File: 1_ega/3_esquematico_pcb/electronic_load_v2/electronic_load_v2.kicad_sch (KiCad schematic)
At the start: 67 parts, among them J1 Encoder, J11 LOAD, J12 Memoria SD, J13 LCD, J15 VCC, J16 RTC, J17 EGB, J3 GND, J6 RPico PWR, J7 GND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

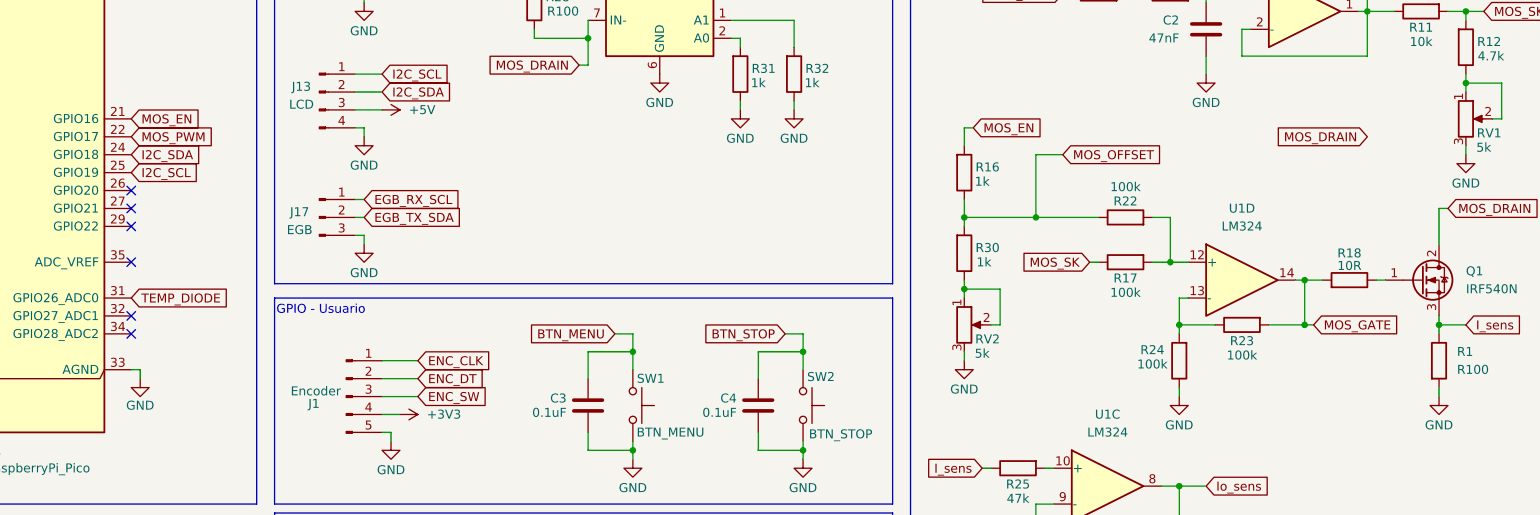
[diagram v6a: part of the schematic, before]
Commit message: add: change Rsense to ina smd size
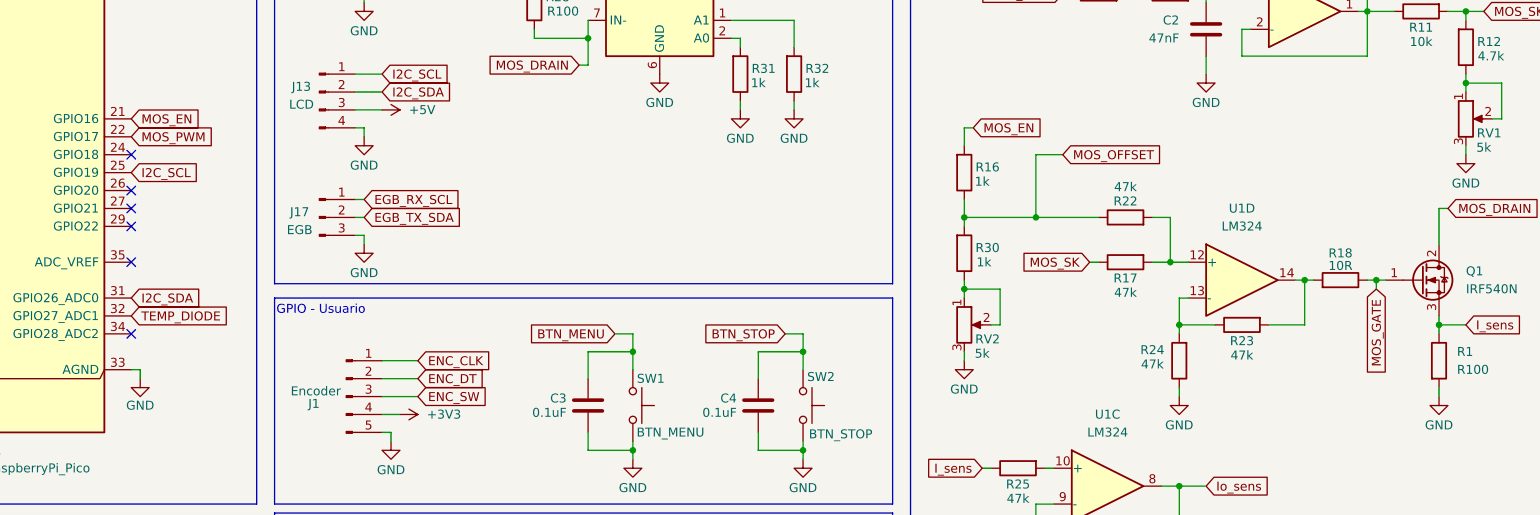
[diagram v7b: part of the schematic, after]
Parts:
- R1: footprint Resistor_THT:R_Axial_DIN0922_L20.0mm_D9.0mm_P25.40mm_Horizontal -> electronic_load:R_shunt_ina219
- R17, R22, R23, R24: value 100k -> 47k
- R20, R21: footprint Resistor_THT:R_Axial_DIN0207_L6.3mm_D2.5mm_P7.62mm_Horizontal -> Resistor_THT:R_Axial_DIN0207_L6.3mm_D2.5mm_P10.16mm_Horizontal
- R31, R32: footprint Resistor_SMD:R_0805_2012Metric_Pad1.20x1.40mm_HandSolder -> Resistor_SMD:R_1206_3216Metric_Pad1.30x1.75mm_HandSolder
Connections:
- net I2C_SDA: now also A1.31 (GPIO26_ADC0); no longer A1.24 (GPIO18)
- net MOS_GATE: now also Q1.1 (G), R18.1; no longer R18.2, R23.2, U1.14
- net TEMP_DIODE: now also A1.32 (GPIO27_ADC1); no longer A1.31 (GPIO26_ADC0)
- new net: R18.2, R23.2, U1.14
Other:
- moved on the sheet: R18
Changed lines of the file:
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@@
 	)
 	(junction
-		(at 67.31 127)
+		(at 254 72.39)
 		(diameter 0)
 		(color 0 0 0 0)
 	)
 	(junction
-		(at 243.84 78.74)
+		(at 67.31 127)
 		(diameter 0)
 		(color 0 0 0 0)
@@
 	)
 	(no_connect
-		(at 77.47 77.47)
-	)
-	(no_connect
 		(at 77.47 80.01)
 	)
@@
 	)
 	(no_connect
+		(at 77.47 54.61)
+	)
+	(no_connect
 		(at 77.47 69.85)
 	)
@@
 	(wire
 		(pts
+			(xy 254 72.39) (xy 255.27 72.39)
+		)
+		(stroke
+			(width 0)
+			(type default)
+		)
+	)
+	(wire
+		(pts
 			(xy 226.06 88.9) (xy 226.06 87.63)
 		)
@@
 	(wire
 		(pts
-			(xy 243.84 72.39) (xy 246.38 72.39)
+			(xy 243.84 72.39) (xy 245.11 72.39)
 		)
 		(stroke
@@
 	(wire
 		(pts
+			(xy 254 72.39) (xy 254 73.66)
+		)
+		(stroke
+			(width 0)
+			(type default)
+		)
+	)
+	(wire
+		(pts
 			(xy 54.61 115.57) (xy 54.61 116.84)
 		)
@@
 	(wire
 		(pts
-			(xy 254 72.39) (xy 255.27 72.39)
+			(xy 252.73 72.39) (xy 254 72.39)
 		)
 		(stroke
@@
 	(wire
 		(pts
-			(xy 243.84 78.74) (xy 245.11 78.74)
-		)
-		(stroke
-			(width 0)
-			(type default)
-		)
-	)
-	(wire
-		(pts
 			(xy 262.89 78.74) (xy 262.89 80.01)
 		)
@@
 	(global_label "I2C_SDA"
 		(shape input)
-		(at 77.47 54.61 0)
+		(at 77.47 74.93 0)
 		(fields_autoplaced yes)
 		(effects
@@
 		)
 		(property "Intersheetrefs" "${INTERSHEET_REFS}"
-			(at 88.0752 54.61 0)
+			(at 88.0752 74.93 0)
 			(effects
 				(font
@@
 		)
 	)
-	(global_label "MOS_DRAIN"
-		(shape input)
-		(at 252.73 52.07 180)
-		(fields_autoplaced yes)
-		(effects
-			(font
-				(size 1.27 1.27)
-			)
-			(justify right)
-		)
-		(property "Intersheetrefs" "${INTERSHEET_REFS}"
-			(at 239.2219 52.07 0)
-			(effects
-				(font
-					(size 1.27 1.27)
-				)
-				(justify right)
-				(hide yes)
-			)
-		)
-	)
 	(global_label "I_sens"
 		(shape input)
@@
 	(global_label "MOS_GATE"
 		(shape input)
-		(at 245.11 78.74 0)
+		(at 254 73.66 270)
 		(fields_autoplaced yes)
 		(effects
@@
 				(size 1.27 1.27)
 			)
-			(justify left)
+			(justify right)
 		)
 		(property "Intersheetrefs" "${INTERSHEET_REFS}"
-			(at 257.5294 78.74 0)
+			(at 254 86.0794 90)
 			(effects
 				(font
 					(size 1.27 1.27)
 				)
-				(justify left)
+				(justify right)
 				(hide yes)
 			)
@@
 	(global_label "TEMP_DIODE"
 		(shape input)
-		(at 77.47 74.93 0)
+		(at 77.47 77.47 0)
 		(fields_autoplaced yes)
 		(effects
@@
 		)
 		(property "Intersheetrefs" "${INTERSHEET_REFS}"
-			(at 91.8851 74.93 0)
+			(at 91.8851 77.47 0)
 			(effects
 				(font
@@
 			)
 		)
-		(property "Value" "100k"
+		(property "Value" "47k"
 			(at 234.95 83.058 90)
 			(effects
@@
 			)
 		)
-		(property "Footprint" "Resistor_SMD:R_0805_2012Metric_Pad1.20x1.40mm_HandSolder"
+		(property "Footprint" "Resistor_SMD:R_1206_3216Metric_Pad1.30x1.75mm_HandSolder"
 			(at 169.672 43.18 90)
 			(effects
@@
 			)
 		)
-		(property "Value" "100k"
+		(property "Value" "47k"
 			(at 222.25 84.328 0)
 			(effects
@@
 			)
 		)
-		(property "Value" "100k"
+		(property "Value" "47k"
 			(at 218.44 59.182 90)
 			(effects
@@
 			)
 		)
-		(property "Footprint" "Resistor_THT:R_Axial_DIN0922_L20.0mm_D9.0mm_P25.40mm_Horizontal"
+		(property "Footprint" "electronic_load:R_shunt_ina219"
 			(at 261.112 83.82 90)
 			(effects
@@
 			)
 		)
-		(property "Value" "100k"
+		(property "Value" "47k"
 			(at 218.44 74.168 90)
 			(effects
@@
 	(symbol
 		(lib_id "Device:R")
-		(at 250.19 72.39 270)
+		(at 248.92 72.39 270)
 		(mirror x)
 		(unit 1)
@@
 		(dnp no)
 		(property "Reference" "R18"
-			(at 250.19 68.58 90)
+			(at 248.92 68.58 90)
 			(effects
 				(font
@@
 		)
 		(property "Value" "10R"
-			(at 250.19 70.358 90)
+			(at 248.92 70.358 90)
 			(effects
 				(font
@@
 		)
 		(property "Footprint" "Resistor_SMD:R_1206_3216Metric_Pad1.30x1.75mm_HandSolder"
-			(at 250.19 74.168 90)
+			(at 248.92 74.168 90)
 			(effects
 				(font
@@
 		)
 		(property "Datasheet" "~"
-			(at 250.19 72.39 0)
+			(at 248.92 72.39 0)
 			(effects
 				(font
@@
 		)
 		(property "Description" "Resistor"
-			(at 250.19 72.39 0)
+			(at 248.92 72.39 0)
 			(effects
 				(font
@@
 			)
 		)
-		(property "Footprint" "Resistor_SMD:R_0805_2012Metric_Pad1.20x1.40mm_HandSolder"
+		(property "Footprint" "Resistor_SMD:R_1206_3216Metric_Pad1.30x1.75mm_HandSolder"
 			(at 162.052 43.18 90)
 			(effects
@@
 			)
 		)
-		(property "Footprint" "Resistor_THT:R_Axial_DIN0207_L6.3mm_D2.5mm_P7.62mm_Horizontal"
+		(property "Footprint" "Resistor_THT:R_Axial_DIN0207_L6.3mm_D2.5mm_P10.16mm_Horizontal"
 			(at 215.392 128.27 90)
 			(effects
@@
 			)
 		)
-		(property "Footprint" "Resistor_THT:R_Axial_DIN0207_L6.3mm_D2.5mm_P7.62mm_Horizontal"
+		(property "Footprint" "Resistor_THT:R_Axial_DIN0207_L6.3mm_D2.5mm_P10.16mm_Horizontal"
 			(at 235.712 128.27 90)
 			(effects

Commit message: chore: add name and logo
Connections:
- net I2C_SDA: now also A1.24 (GPIO18); no longer A1.31 (GPIO26_ADC0)
- net TEMP_DIODE: now also A1.31 (GPIO26_ADC0); no longer A1.32 (GPIO27_ADC1)
